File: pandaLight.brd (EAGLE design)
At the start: 160 x 100 mm, 161 parts, among them J1 PJ-037A, U1 MIC23450AAAYML, U10 AS4C128M16D3, U11 PMOD-2X6, U12 PMOD-2X6, U13 PLR135-T10, U14 PLT133-T10W, U15 PLR135-T10, U16 TP10SQ, U17 TP10SQ, U18 PAN1322, U2 6SLX45CSG324, U3 TPD4S014SON, U4 FT2232HL, U5 93LC46BT-I/OT, U6 TPD12S016PWR, U7 TPD12S016PWR, U8 N25Q128AF8, U9 TPD12S016PWR, X1 USBUB-S, X2 HDMI_RECEPTICAL_A, X3 HDMI_RECEPTICAL_A, X4 HDMI_RECEPTICAL_A, Y1 403, Y2 20Mhz

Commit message: Finished first routing of HDMI_RX1; Corrected some traces and placements
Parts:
- moved C33 120.7 mm to (22.6, 84.5), turned to 180 degrees
- moved R19 6.20 mm to (9.08, 75.5), turned to 45 degrees
- moved C25 2.91 mm to (25.6, 83.2), turned to 0 degrees
- moved C21 1.75 mm to (22.2, 70.2)
- moved C22 1.75 mm to (18.8, 70.2)
- moved C23 1.75 mm to (27.2, 79.0)
- moved C24 1.75 mm to (19.5, 84.5)
- moved C27 1.75 mm to (27.2, 74.8)
- moved C31 1.75 mm to (6.62, 80.2)
- moved C32 1.75 mm to (11.0, 77.9)
- moved C34 1.75 mm to (5.25, 73.0)
- moved C35 1.75 mm to (11.3, 81.1)
- moved C36 1.75 mm to (9.25, 83.7)
- moved C37 1.75 mm to (8.75, 87.0)
- moved FB2 1.75 mm to (5.03, 80.9)
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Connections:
- net HDMI_RX1_CEC_3V3: now also U2.G18; no longer U2.M16
- net HDMI_RX1_CTRL_EN: now also U2.J18; no longer U2.N18
- net HDMI_RX1_SCL_3V3: now also U2.H17; no longer U2.M18
- net HDMI_RX1_SDA_3V3: now also U2.H18; no longer U2.N17
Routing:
- net HDMI_RX1_CTRL_EN: track 7.43 -> 43.3 mm, vias 2 -> 3
- net HDMI_RX1_SCL_3V3: track 9.54 -> 37.8 mm
- net HDMI_RX1_SDA_3V3: track 9.40 -> 37.6 mm
- net HDMI_RX1_CEC_3V3: track 9.75 -> 36.1 mm
- net USB_5V_DISABLE: track 11.5 -> 2.77 mm, vias 2 -> 0
- net HDMI_RX1_DATA1_P: track 22.1 -> 26.8 mm
- net HDMI_RX1_DATA1_N: track 22.2 -> 26.8 mm
- net USB_5V_ACK#: track 6.25 -> 2.51 mm
- net +3V3: track 52.4 -> 55.7 mm, vias 22 -> 25
- net +1V8: track 12.0 -> 9.25 mm
- net HDMI_RX1_DATA0_N: track 24.9 -> 26.8 mm
- net GND: track 105.8 -> 104.3 mm, vias 79 -> 82
- net HDMI_RX1_DATA0_P: track 25.7 -> 26.8 mm
- net HDMI_RX0_CTRL_EN: track 25.6 -> 24.5 mm
- net USB_TMS: track 5.95 -> 4.96 mm
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- removed copper zone on layer 1, net N$31
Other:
- board size 160 x 100 mm -> 161.8 x 100 mm

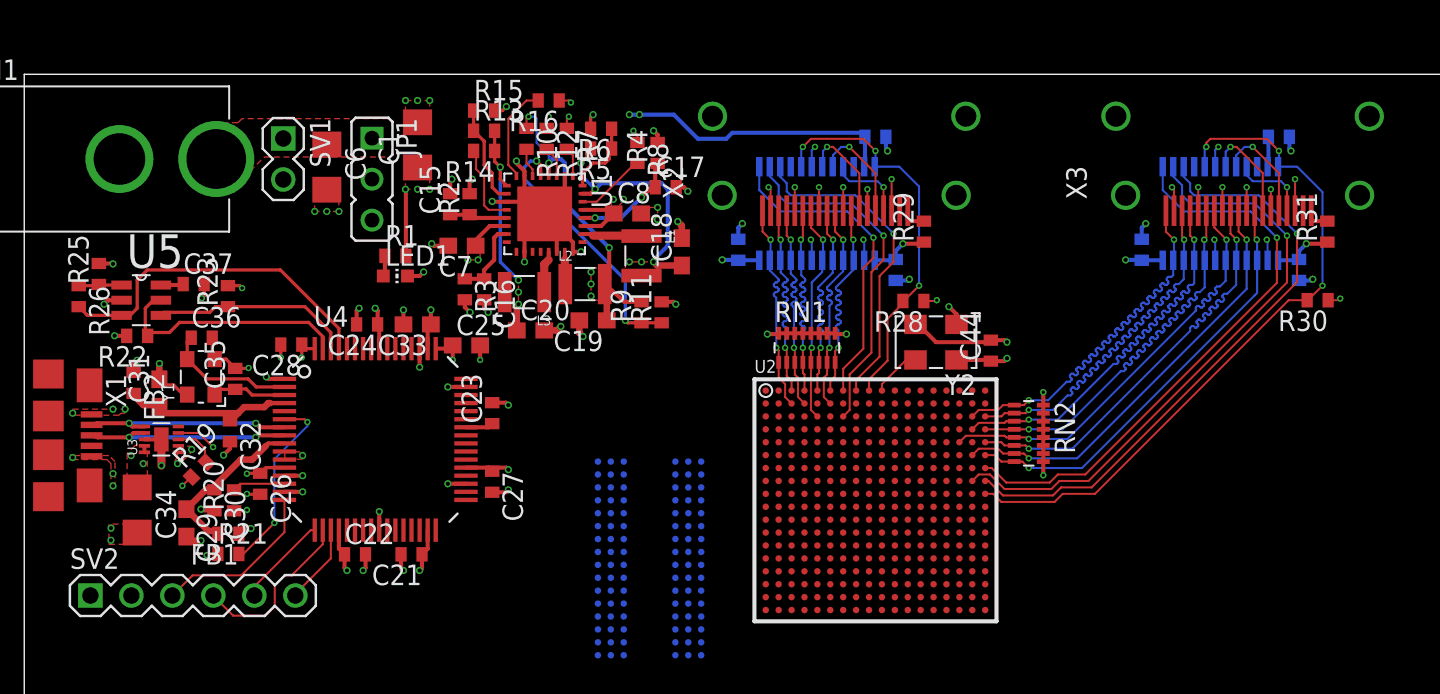
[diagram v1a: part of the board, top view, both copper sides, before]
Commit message: Straightened some via stubs
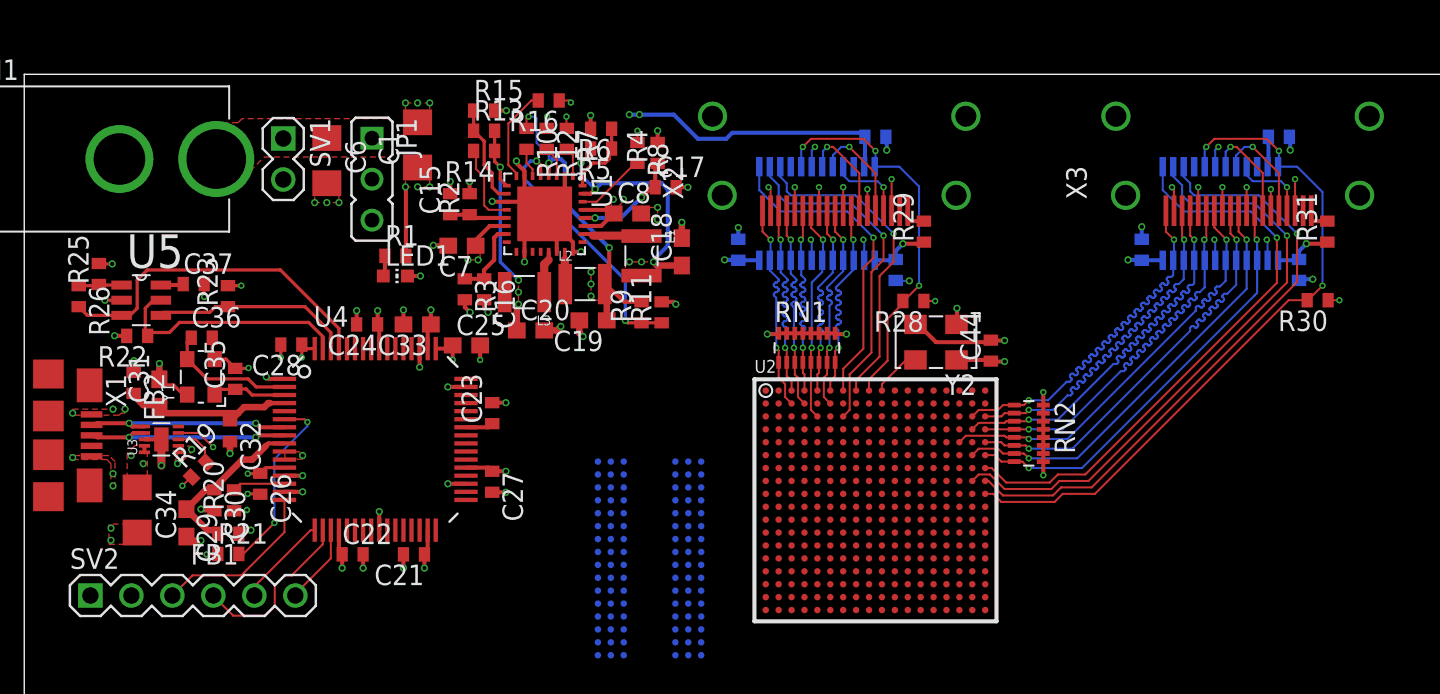
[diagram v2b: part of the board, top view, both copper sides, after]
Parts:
- moved C6 0.40 mm to (17.0, 94.7)
- moved C21 0.15 mm to (22.4, 70.2)
- moved C22 0.15 mm to (18.6, 70.2)
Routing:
- net GND: track 104.3 -> 100.2 mm
- net +3V3: track 55.7 -> 53.7 mm

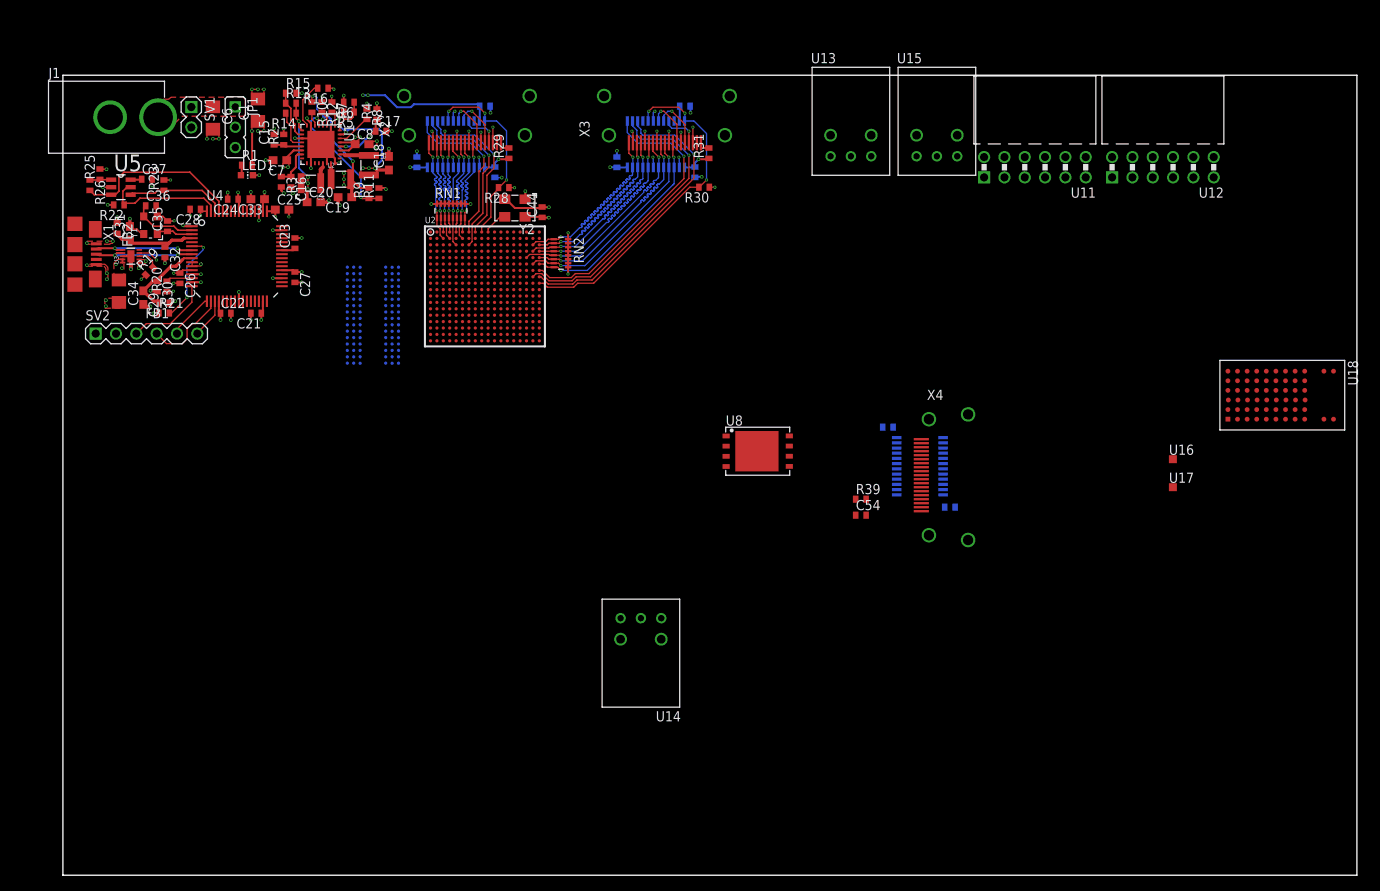
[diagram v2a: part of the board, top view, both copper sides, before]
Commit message: Moved the FPGA to the center of the PCB, which is now 10mm x 5mm in size
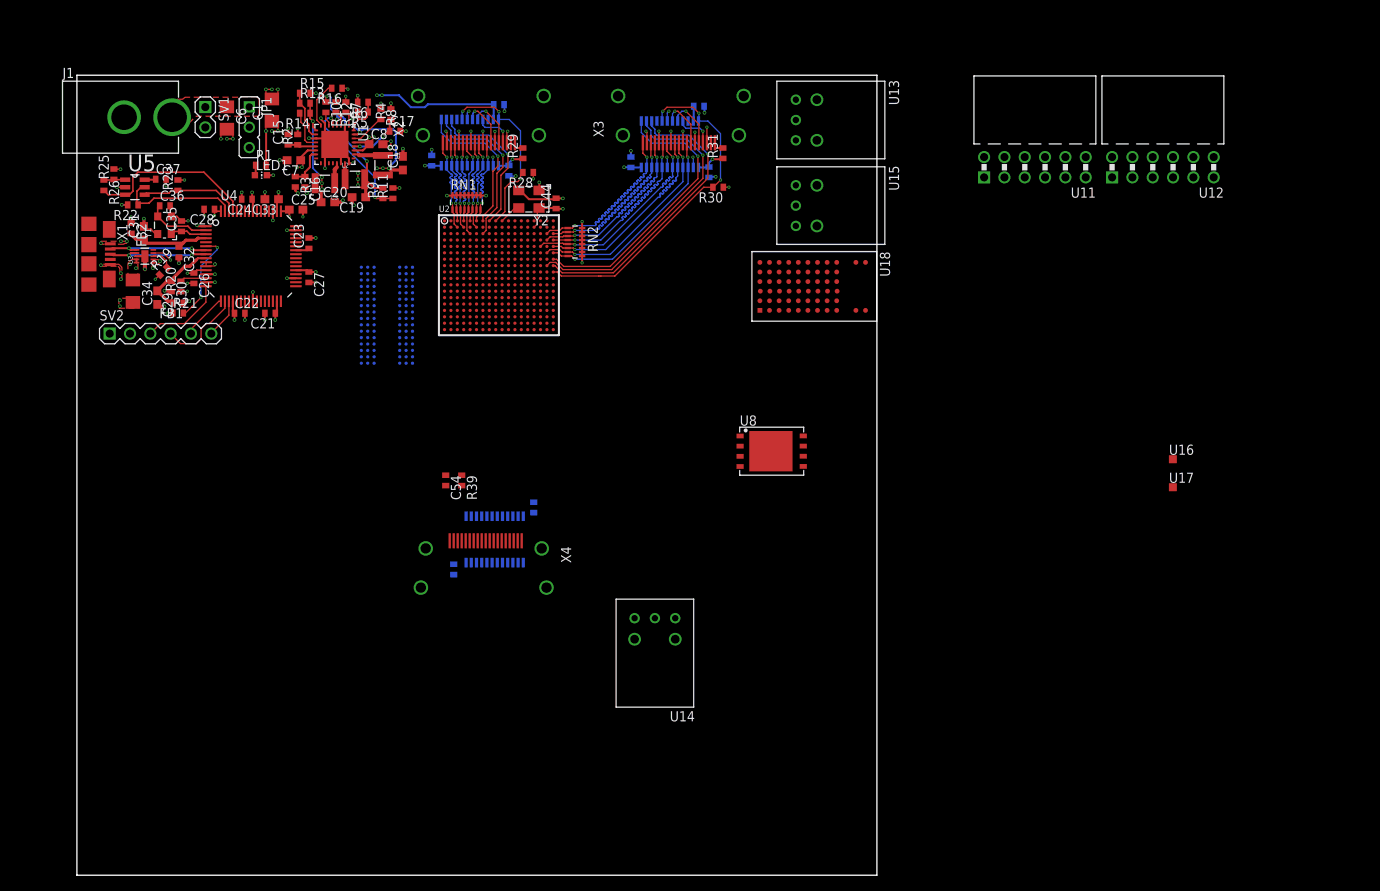
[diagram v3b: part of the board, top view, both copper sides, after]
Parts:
- moved C55 62.5 mm to (47.1, 38.2), turned to 90 degrees
- moved U18 60.1 mm to (92.0, 73.6)
- moved X4 59.7 mm to (51.1, 37.9), turned to 270 degrees
- moved U9 53.9 mm to (52.2, 42.0), turned to 90 degrees
- moved C54 52.1 mm to (46.1, 49.4), turned to 270 degrees
- moved R39 50.0 mm to (48.1, 49.4), turned to 270 degrees
- moved C56 45.4 mm to (57.1, 46.0), turned to 90 degrees
- moved U15 17.4 mm to (92.5, 83.7), turned to 270 degrees
- moved U13 4.66 mm to (92.5, 94.4), turned to 270 degrees
- moved R28 3.59 mm to (56.4, 87.8)
- moved RN2 2.24 mm to (62.2, 79.2)
- moved U2 2.24 mm to (52.8, 75.0)
- moved RN1 2.21 mm to (48.7, 84.1)
- moved C44 2.07 mm to (59.9, 84.0)
- moved Y2 2.07 mm to (56.5, 84.5)
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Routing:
- net +3V3: track 53.7 -> 56.3 mm
- net HDMI_RX0_DATA0_P: track 13.5 -> 12.1 mm
- net HDMI_RX0_DATA2_N: track 13.5 -> 12.1 mm
- net HDMI_RX0_DATA1_P: track 13.4 -> 12.1 mm
- net HDMI_RX0_CLK_P: track 13.5 -> 12.2 mm
- net HDMI_RX0_DATA2_P: track 13.4 -> 12.1 mm
- net HDMI_RX0_DATA0_N: track 13.5 -> 12.1 mm
- net HDMI_RX0_DATA1_N: track 13.4 -> 12.2 mm
- net HDMI_RX0_CLK_N: track 13.4 -> 12.1 mm
- net HDMI_RX0_SCL_3V3: track 21.8 -> 20.6 mm
- net HDMI_RX0_CEC_3V3: track 20.0 -> 18.8 mm
- net HDMI_RX0_SDA_3V3: track 20.1 -> 19.1 mm
- net GND: track 100.2 -> 99.2 mm
- net HDMI_RX1_DATA2_N: track 26.9 -> 26.1 mm
- net HDMI_RX1_DATA1_N: track 26.8 -> 26.0 mm
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- added copper zone on layer 15, net N$32
- added copper zone on layer 2, net N$52
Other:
- board size 161.8 x 100 mm -> 100 x 100 mm

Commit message: Actually resized the board; Tweaked some FT223H related traces
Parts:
- moved JP3 211.5 mm to (139.1, 32.0)
- moved JP2 193.3 mm to (139.0, 28.3)
- moved C68 189.3 mm to (86.7, 42.5), turned to 90 degrees
- moved C70 185.5 mm to (86.7, 31.9), turned to 90 degrees
- moved L5 150.7 mm to (85.1, 31.9), turned to 270 degrees
- moved L4 140.9 mm to (85.1, 42.5), turned to 270 degrees
- moved R17 59.0 mm to (13.2, 22.2), turned to 0 degrees
- moved R18 58.4 mm to (13.2, 21.1), turned to 0 degrees
- moved R19 51.3 mm to (8.60, 24.2), turned to 90 degrees
- moved RN2 50.0 mm to (61.9, 29.1)
- moved C11 50.0 mm to (-97.8, 52.9)
- moved C12 50.0 mm to (-104.1, 47.8)
- moved C13 50.0 mm to (-17.8, 52.9)
- moved C14 50.0 mm to (-36.8, 52.9)
- moved C3 50.0 mm to (-102.9, 52.9)
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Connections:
- net TOS_IN0: no longer U2.A2
- net TOS_IN1: no longer U2.T18
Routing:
- net +5V: track 34.5 -> 59.4 mm
- net N$11: track 11.6 -> 2.01 mm, vias 2 -> 1
- net USB_5V_ACK#: track 2.51 -> 8.64 mm, vias 1 -> 2
- net GND: track 99.2 -> 104.1 mm, vias 82 -> 90
- net N$4: track 0.00 -> 4.89 mm
- net N$36: track 0.00 -> 4.88 mm
- net N$31: track 10.5 -> 7.52 mm
- net USB_5V_DISABLE: track 2.77 -> 5.15 mm
- net +3V3: track 56.3 -> 58.0 mm, vias 25 -> 31
- net USB_TDI: track 5.75 -> 4.19 mm
- net USB_TCK: track 10.6 -> 9.02 mm
- net USB_TMS: track 4.96 -> 3.41 mm
- net USB_TDO: track 10.8 -> 9.24 mm
- net N$13: track 3.28 -> 1.99 mm, vias 0 -> 1
- net HDMI_RX1_CTRL_EN: track 42.6 -> 43.5 mm
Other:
- board size 100 x 100 mm -> 100 x 50 mm

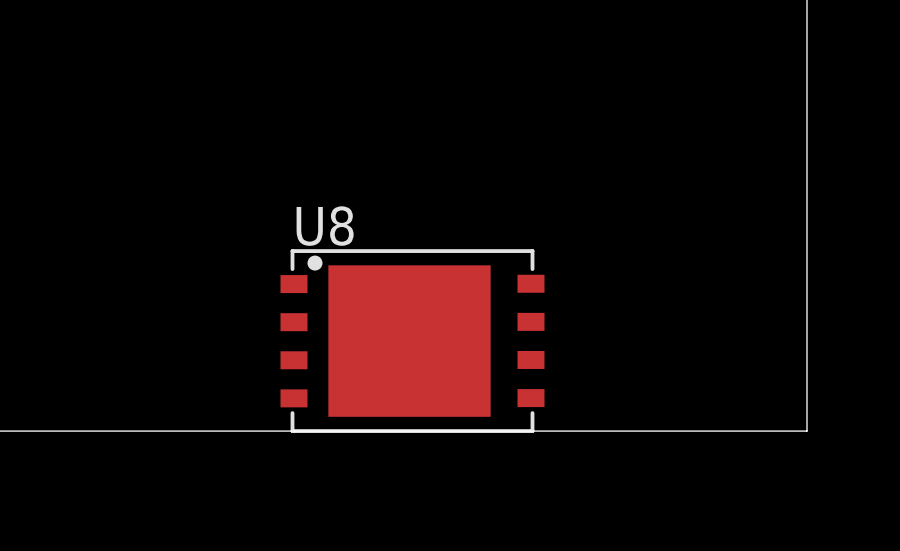
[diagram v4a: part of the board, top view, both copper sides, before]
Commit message: Set polygon sizes from 0 to 5mil (for later GERBER generation)
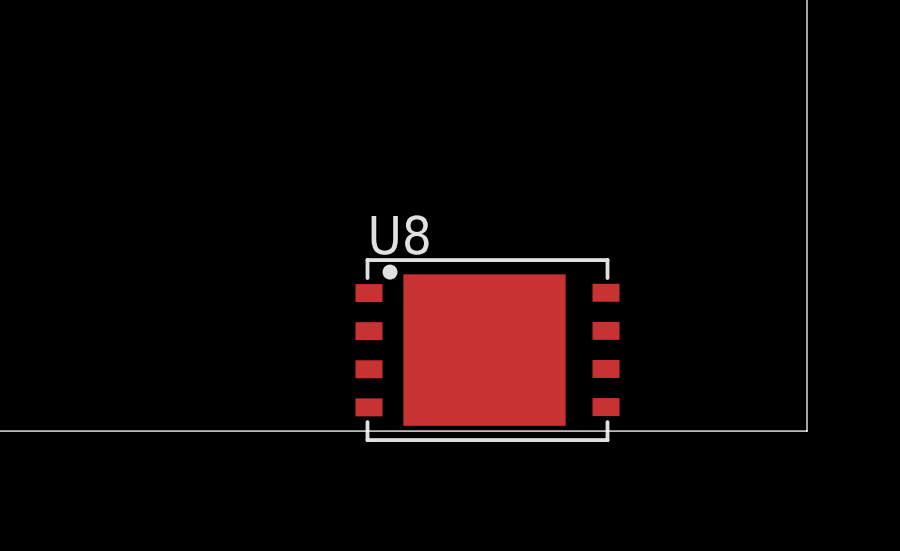
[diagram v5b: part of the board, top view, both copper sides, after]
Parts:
- moved U8 2.52 mm to (89.2, 2.70)
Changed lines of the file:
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@@
 <layers>
 <layer number="1" name="Top" color="2" fill="1" visible="yes" active="yes"/>
-<layer number="2" name="Ground" color="1" fill="1" visible="no" active="yes"/>
+<layer number="2" name="Ground" color="1" fill="1" visible="yes" active="yes"/>
 <layer number="3" name="Route3" color="4" fill="3" visible="no" active="no"/>
 <layer number="4" name="Route4" color="1" fill="4" visible="no" active="no"/>
@@
 <layer number="13" name="Route13" color="4" fill="5" visible="no" active="no"/>
 <layer number="14" name="Route14" color="1" fill="6" visible="no" active="no"/>
-<layer number="15" name="Power" color="4" fill="1" visible="no" active="yes"/>
+<layer number="15" name="Power" color="4" fill="1" visible="yes" active="yes"/>
 <layer number="16" name="Bottom" color="3" fill="1" visible="yes" active="yes"/>
 <layer number="17" name="Pads" color="2" fill="1" visible="yes" active="yes"/>
@@
 <param name="layerSetup" value="(1*2+15*16)"/>
 <param name="mtCopper" value="0.035mm 0.035mm 0.035mm 0.035mm 0.035mm 0.035mm 0.035mm 0.035mm 0.035mm 0.035mm 0.035mm 0.035mm 0.035mm 0.035mm 0.035mm 0.035mm"/>
-<param name="mtIsolate" value="0.2mm 1.5mm 0.2mm 0.15mm 0.2mm 0.15mm 0.2mm 0.15mm 0.2mm 0.15mm 0.2mm 0.15mm 0.2mm 0.15mm 0.2mm"/>
+<param name="mtIsolate" value="0.15mm 1.16mm 0.2mm 0.15mm 0.2mm 0.15mm 0.2mm 0.15mm 0.2mm 0.15mm 0.2mm 0.15mm 0.2mm 0.15mm 0.15mm"/>
 <param name="mdWireWire" value="5mil"/>
 <param name="mdWirePad" value="5mil"/>
@@
 <attribute name="PARTNO" value="ERJ-2RKF1002X" x="48.3" y="14.15" size="1.778" layer="27" rot="R270" display="off"/>
 </element>
-<element name="U8" library="pandaLight" package="V-PDFN-8_8X6" value="N25Q128AF8" x="86.75" y="3">
-<attribute name="PARTNO" value="N25Q128A13EF840E" x="86.75" y="3" size="1.778" layer="27" display="off"/>
+<element name="U8" library="pandaLight" package="V-PDFN-8_8X6" value="N25Q128AF8" x="89.25" y="2.7">
+<attribute name="PARTNO" value="N25Q128A13EF840E" x="89.25" y="2.7" size="1.778" layer="27" display="off"/>
 </element>
 <element name="R32" library="pandaLight" package="0402" value="2.4k" x="-86.36" y="30.01">
@@
 <wire x1="35.55" y1="26" x2="35.55" y2="24.4" width="0" layer="19" extent="16-16"/>
 <wire x1="57" y1="13.325" x2="52.45" y2="11.525" width="0" layer="19" extent="16-16"/>
-<wire x1="82.9" y1="1.09" x2="85.375" y2="20.605" width="0" layer="19" extent="1-1"/>
+<wire x1="85.4" y1="0.79" x2="85.375" y2="20.605" width="0" layer="19" extent="1-1"/>
 <wire x1="-17.13" y1="52.87" x2="5.9" y2="44.75" width="0" layer="19" extent="1-1"/>
 <wire x1="-23.48" y1="52.87" x2="-17.13" y2="52.87" width="0" layer="19" extent="1-1"/>
@@
 <wire x1="57" y1="12.025" x2="56.35" y2="19" width="0" layer="19" extent="1-16"/>
 <wire x1="55.7" y1="11.525" x2="57" y2="12.025" width="0" layer="19" extent="16-16"/>
-<wire x1="90.8" y1="4.91" x2="90.175" y2="20.605" width="0" layer="19" extent="1-1"/>
+<wire x1="93.3" y1="4.61" x2="91.375" y2="20.605" width="0" layer="19" extent="1-1"/>
 <wire x1="-18.43" y1="52.87" x2="4.625" y2="38.275" width="0" layer="19" extent="1-1"/>
 <wire x1="-17.16" y1="63.03" x2="-18.43" y2="52.87" width="0" layer="19" extent="1-1"/>
@@
 <contactref element="U8" pad="1"/>
 <contactref element="R32" pad="1"/>
-<wire x1="47.55" y1="18.2" x2="82.9" y2="4.9" width="0" layer="19" extent="1-1"/>
+<wire x1="47.55" y1="18.2" x2="85.4" y2="4.6" width="0" layer="19" extent="1-1"/>
 <wire x1="-87.01" y1="30.01" x2="47.55" y2="18.2" width="0" layer="19" extent="1-1"/>
 </signal>
@@
 <contactref element="R34" pad="1"/>
 <contactref element="R38" pad="2"/>
-<wire x1="57.15" y1="20.6" x2="90.8" y2="2.37" width="0" layer="19" extent="1-1"/>
+<wire x1="57.15" y1="20.6" x2="93.3" y2="2.07" width="0" layer="19" extent="1-1"/>
 <wire x1="-93.36" y1="37.63" x2="57.15" y2="20.6" width="0" layer="19" extent="1-1"/>
 <wire x1="-97.14" y1="37.63" x2="-93.36" y2="37.63" width="0" layer="19" extent="1-1"/>
@@
 <contactref element="U2" pad="T13"/>
 <contactref element="U8" pad="5"/>
-<wire x1="55.55" y1="19.8" x2="90.8" y2="1.1" width="0" layer="19" extent="1-1"/>
+<wire x1="55.55" y1="19.8" x2="93.3" y2="0.8" width="0" layer="19" extent="1-1"/>
 </signal>
 <signal name="N$43">
 <contactref element="U8" pad="2"/>
 <contactref element="U2" pad="R13"/>
-<wire x1="55.55" y1="20.6" x2="82.9" y2="3.63" width="0" layer="19" extent="1-1"/>
+<wire x1="55.55" y1="20.6" x2="85.4" y2="3.33" width="0" layer="19" extent="1-1"/>
 </signal>
 <signal name="N$44">
@@
 <contactref element="U2" pad="T14"/>
 <contactref element="R35" pad="1"/>
-<wire x1="56.35" y1="19.8" x2="82.9" y2="2.36" width="0" layer="19" extent="1-1"/>
+<wire x1="56.35" y1="19.8" x2="85.4" y2="2.06" width="0" layer="19" extent="1-1"/>
 <wire x1="-83.2" y1="37.63" x2="56.35" y2="19.8" width="0" layer="19" extent="1-1"/>
 </signal>
@@
 <contactref element="U8" pad="7"/>
 <contactref element="R33" pad="1"/>
-<wire x1="56.35" y1="18.2" x2="90.8" y2="3.64" width="0" layer="19" extent="1-1"/>
+<wire x1="56.35" y1="18.2" x2="93.3" y2="3.34" width="0" layer="19" extent="1-1"/>
 <wire x1="-88.28" y1="37.63" x2="56.35" y2="18.2" width="0" layer="19" extent="1-1"/>
 </signal>
@@
 </signal>
 <signal name="N$32">
-<polygon width="0" layer="15" pour="cutout" thermals="no">
+<polygon width="0.127" layer="15" pour="cutout" thermals="no">
 <vertex x="96.95" y="26.15"/>
 <vertex x="100" y="26.15"/>
@@
 </signal>
 <signal name="N$52">
-<polygon width="0" layer="2" pour="cutout" thermals="no">
+<polygon width="0.127" layer="2" pour="cutout" thermals="no">
 <vertex x="96.95" y="26.15"/>
 <vertex x="100" y="26.15"/>
